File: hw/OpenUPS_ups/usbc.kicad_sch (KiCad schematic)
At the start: 12 parts, among them J1001 USB4105-GF-A, Q601 2N7002, U1001 MCP6547, U1002 AP22814BW5

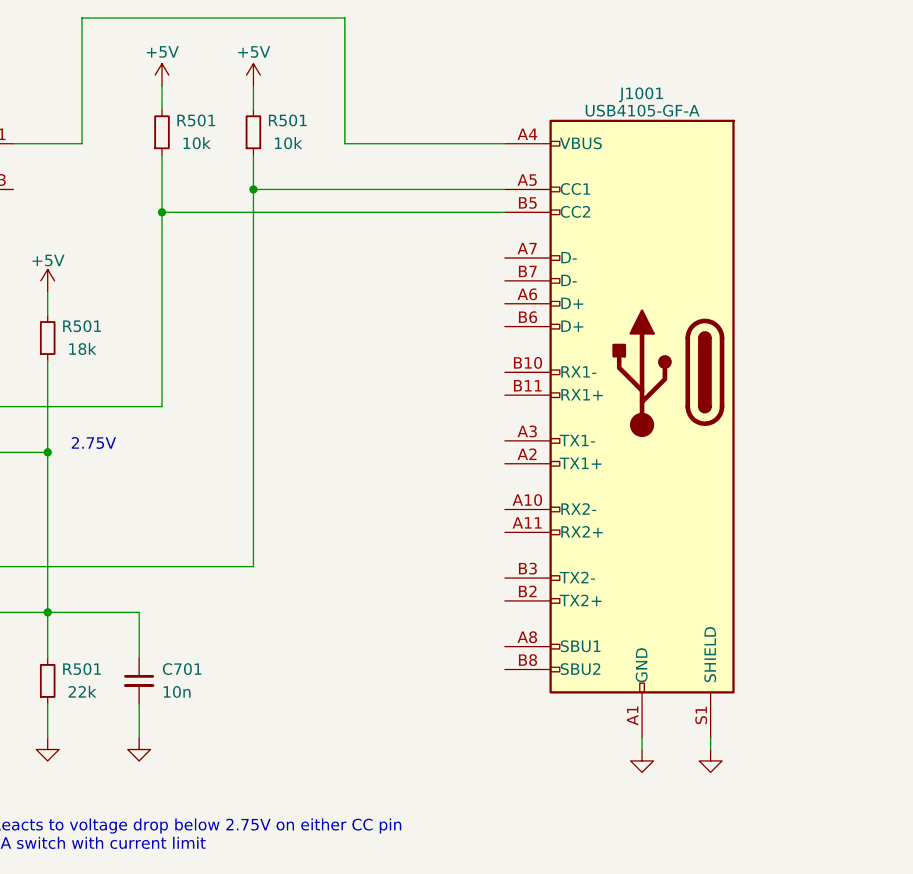
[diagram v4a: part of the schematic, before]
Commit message: Issue #22 ESD protection on USB, Bat Data, Fans
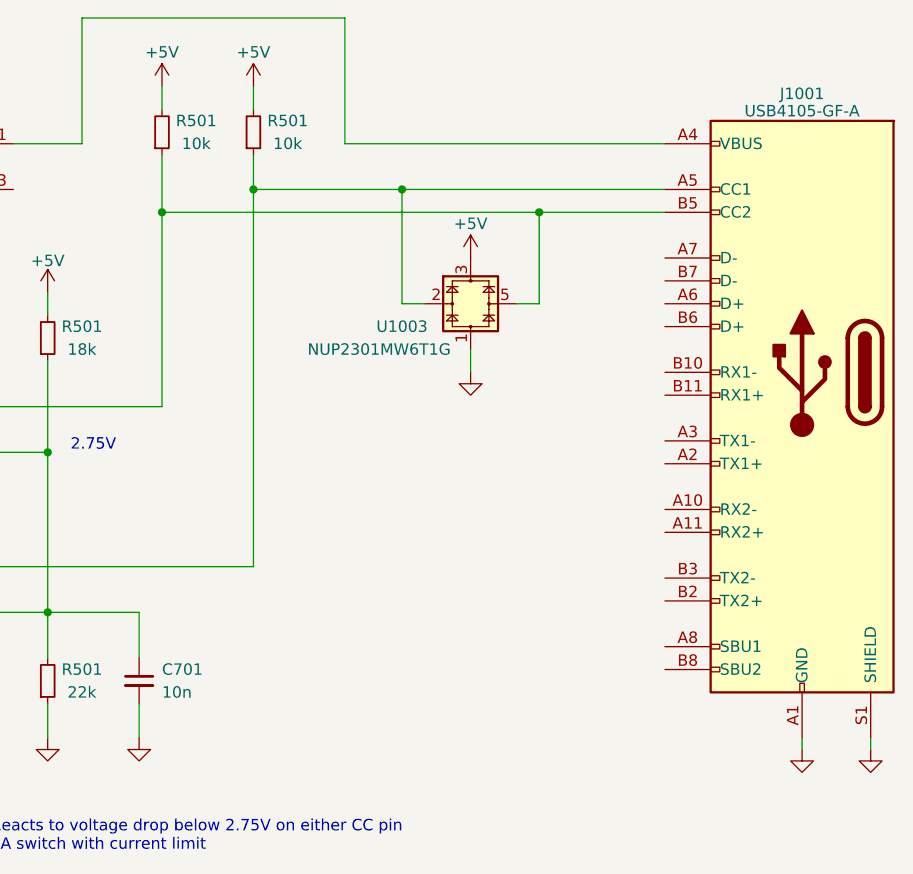
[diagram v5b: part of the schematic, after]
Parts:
- added U1003: NUP2301MW6T1G, Package_TO_SOT_SMD:SOT-363_SC-70-6, symbol OpenUPS_ups:NUP2301MW6T1G
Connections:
- net +5V: now also U1003.3
- net GND: now also U1003.1
- net at J1001.A5 (CC1), R501.1, U1001.5 (+): now also U1003.2
- net at J1001.B5 (CC2), R501.1, U1001.3 (+): now also U1003.5
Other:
- moved on the sheet: J1001
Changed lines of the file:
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@@
   (junction (at 66.04 80.01) (diameter 0) (color 0 0 0 0)
   )
+  (junction (at 137.16 35.56) (diameter 0) (color 0 0 0 0)
+  )
   (junction (at 66.04 38.1) (diameter 0) (color 0 0 0 0)
   )
@@
   (junction (at 97.79 64.77) (diameter 0) (color 0 0 0 0)
   )
+  (junction (at 152.4 38.1) (diameter 0) (color 0 0 0 0)
+  )
   (junction (at 66.04 27.94) (diameter 0) (color 0 0 0 0)
   )
@@
     (stroke (width 0) (type default))
   )
+  (wire (pts (xy 149.86 48.26) (xy 152.4 48.26))
+    (stroke (width 0) (type default))
+  )
   (wire (pts (xy 101.6 16.51) (xy 101.6 30.48))
     (stroke (width 0) (type default))
@@
     (stroke (width 0) (type default))
   )
+  (wire (pts (xy 137.16 35.56) (xy 166.37 35.56))
+    (stroke (width 0) (type default))
+  )
+  (wire (pts (xy 152.4 48.26) (xy 152.4 38.1))
+    (stroke (width 0) (type default))
+  )
   (wire (pts (xy 110.49 31.75) (xy 110.49 38.1))
     (stroke (width 0) (type default))
@@
     (stroke (width 0) (type default))
   )
-  (wire (pts (xy 148.59 30.48) (xy 130.81 30.48))
+  (wire (pts (xy 137.16 48.26) (xy 137.16 35.56))
+    (stroke (width 0) (type default))
+  )
+  (wire (pts (xy 166.37 30.48) (xy 130.81 30.48))
     (stroke (width 0) (type default))
   )
@@
     (stroke (width 0) (type default))
   )
-  (wire (pts (xy 163.83 96.52) (xy 163.83 97.79))
+  (wire (pts (xy 181.61 96.52) (xy 181.61 97.79))
     (stroke (width 0) (type default))
   )
@@
     (stroke (width 0) (type default))
   )
-  (wire (pts (xy 171.45 96.52) (xy 171.45 97.79))
+  (wire (pts (xy 189.23 96.52) (xy 189.23 97.79))
     (stroke (width 0) (type default))
   )
@@
     (stroke (width 0) (type default))
   )
+  (wire (pts (xy 139.7 48.26) (xy 137.16 48.26))
+    (stroke (width 0) (type default))
+  )
   (wire (pts (xy 107.95 87.63) (xy 107.95 82.55))
     (stroke (width 0) (type default))
@@
     (stroke (width 0) (type default))
   )
+  (wire (pts (xy 144.78 53.34) (xy 144.78 55.88))
+    (stroke (width 0) (type default))
+  )
   (wire (pts (xy 66.04 22.86) (xy 66.04 27.94))
     (stroke (width 0) (type default))
@@
     (stroke (width 0) (type default))
   )
-  (wire (pts (xy 120.65 35.56) (xy 148.59 35.56))
+  (wire (pts (xy 120.65 35.56) (xy 137.16 35.56))
     (stroke (width 0) (type default))
   )
@@
     (stroke (width 0) (type default))
   )
-  (wire (pts (xy 110.49 38.1) (xy 148.59 38.1))
+  (wire (pts (xy 110.49 38.1) (xy 152.4 38.1))
+    (stroke (width 0) (type default))
+  )
+  (wire (pts (xy 152.4 38.1) (xy 166.37 38.1))
     (stroke (width 0) (type default))
   )
@@
     )
   )
-  (symbol (lib_id "power:GND") (at 171.45 97.79 0) (unit 1)
-    (in_bom yes) (on_board yes) (dnp no)
-    (property "Reference" "#PWR0306" (at 171.45 104.14 0)
-      (effects (font (size 1.27 1.27)) hide)
-    )
-    (property "Value" "GND" (at 171.45 101.6 0)
-      (effects (font (size 1.27 1.27)) hide)
-    )
-    (property "Footprint" "" (at 171.45 97.79 0)
-      (effects (font (size 1.27 1.27)))
-    )
-    (property "Datasheet" "" (at 171.45 97.79 0)
+  (symbol (lib_id "power:GND") (at 189.23 97.79 0) (unit 1)
+    (in_bom yes) (on_board yes) (dnp no)
+    (property "Reference" "#PWR0306" (at 189.23 104.14 0)
+      (effects (font (size 1.27 1.27)) hide)
+    )
+    (property "Value" "GND" (at 189.23 101.6 0)
+      (effects (font (size 1.27 1.27)) hide)
+    )
+    (property "Footprint" "" (at 189.23 97.79 0)
+      (effects (font (size 1.27 1.27)))
+    )
+    (property "Datasheet" "" (at 189.23 97.79 0)
       (effects (font (size 1.27 1.27)))
     )
@@
     )
   )
+  (symbol (lib_id "power:+5V") (at 144.78 43.18 0) (unit 1)
+    (in_bom yes) (on_board yes) (dnp no)
+    (property "Reference" "#PWR0128" (at 144.78 46.99 0)
+      (effects (font (size 1.27 1.27)) hide)
+    )
+    (property "Value" "+5V" (at 144.78 39.37 0)
+      (effects (font (size 1.27 1.27)))
+    )
+    (property "Footprint" "" (at 144.78 43.18 0)
+      (effects (font (size 1.27 1.27)) hide)
+    )
+    (property "Datasheet" "" (at 144.78 43.18 0)
+      (effects (font (size 1.27 1.27)) hide)
+    )
+    (pin "1")
+    (instances
+      (project "OpenUPS_ups"
+        (path "/f77faec3-eac4-47f3-a2de-ec4a039f4502"
+          (reference "#PWR0128") (unit 1)
+        )
+        (path "/f77faec3-eac4-47f3-a2de-ec4a039f4502/5d533980-99bb-4871-b1d2-8a68cd48eb84"
+          (reference "#PWR01015") (unit 1)
+        )
+      )
+    )
+  )
+  (symbol (lib_id "power:GND") (at 144.78 55.88 0) (unit 1)
+    (in_bom yes) (on_board yes) (dnp no)
+    (property "Reference" "#PWR0306" (at 144.78 62.23 0)
+      (effects (font (size 1.27 1.27)) hide)
+    )
+    (property "Value" "GND" (at 144.78 59.69 0)
+      (effects (font (size 1.27 1.27)) hide)
+    )
+    (property "Footprint" "" (at 144.78 55.88 0)
+      (effects (font (size 1.27 1.27)))
+    )
+    (property "Datasheet" "" (at 144.78 55.88 0)
+      (effects (font (size 1.27 1.27)))
+    )
+    (pin "1")
+    (instances
+      (project "OpenUPS_ups"
+        (path "/f77faec3-eac4-47f3-a2de-ec4a039f4502/c1f639ea-b62e-4979-b175-523e44c4a4ee"
+          (reference "#PWR0306") (unit 1)
+        )
+        (path "/f77faec3-eac4-47f3-a2de-ec4a039f4502/0bd99307-a15c-41e8-997b-077d576f806c"
+          (reference "#PWR0514") (unit 1)
+        )
+        (path "/f77faec3-eac4-47f3-a2de-ec4a039f4502/8c312927-9c4e-41ad-b941-6f477a792759"
+          (reference "#PWR0805") (unit 1)
+        )
+        (path "/f77faec3-eac4-47f3-a2de-ec4a039f4502"
+          (reference "#PWR0129") (unit 1)
+        )
+        (path "/f77faec3-eac4-47f3-a2de-ec4a039f4502/5d533980-99bb-4871-b1d2-8a68cd48eb84"
+          (reference "#PWR01016") (unit 1)
+        )
+      )
+    )
+  )
   (symbol (lib_id "Device:R_Small") (at 120.65 29.21 0) (mirror x) (unit 1)
     (in_bom yes) (on_board yes) (dnp no)
@@
     )
   )
-  (symbol (lib_id "Connector:USB_C_Receptacle") (at 163.83 55.88 0) (mirror y) (unit 1)
-    (in_bom yes) (on_board yes) (dnp no)
-    (property "Reference" "J1001" (at 163.83 24.9301 0)
-      (effects (font (size 1.27 1.27)))
-    )
-    (property "Value" "USB4105-GF-A" (at 163.83 26.8511 0)
-      (effects (font (size 1.27 1.27)))
-    )
-    (property "Footprint" "Connector_USB:USB_C_Receptacle_GCT_USB4105-xx-A_16P_TopMnt_Horizontal" (at 160.02 55.88 0)
-      (effects (font (size 1.27 1.27)) hide)
-    )
-    (property "Datasheet" "" (at 160.02 55.88 0)
+  (symbol (lib_id "Connector:USB_C_Receptacle") (at 181.61 55.88 0) (mirror y) (unit 1)
+    (in_bom yes) (on_board yes) (dnp no)
+    (property "Reference" "J1001" (at 181.61 24.9301 0)
+      (effects (font (size 1.27 1.27)))
+    )
+    (property "Value" "USB4105-GF-A" (at 181.61 26.8511 0)
+      (effects (font (size 1.27 1.27)))
+    )
+    (property "Footprint" "Connector_USB:USB_C_Receptacle_GCT_USB4105-xx-A_16P_TopMnt_Horizontal" (at 177.8 55.88 0)
+      (effects (font (size 1.27 1.27)) hide)
+    )
+    (property "Datasheet" "" (at 177.8 55.88 0)
       (effects (font (size 1.27 1.27)) hide)
     )
@@
     )
   )
+  (symbol (lib_id "OpenUPS_ups:NUP2301MW6T1G") (at 144.78 44.45 0) (unit 1)
+    (in_bom yes) (on_board yes) (dnp no)
+    (property "Reference" "U1003" (at 137.16 50.8 0)
+      (effects (font (size 1.27 1.27)))
+    )
+    (property "Value" "NUP2301MW6T1G" (at 134.62 53.34 0)
+      (effects (font (size 1.27 1.27)))
+    )
+    (property "Footprint" "Package_TO_SOT_SMD:SOT-363_SC-70-6" (at 144.78 44.45 0)
+      (effects (font (size 1.27 1.27)) hide)
+    )
+    (property "Datasheet" "https://www.tme.eu/Document/58b5ad97e31b8cb20a2de836acc71031/NUP2301MW6T1G.PDF" (at 144.78 44.45 0)
+      (effects (font (size 1.27 1.27)) hide)
+    )
+    (pin "1")
+    (pin "2")
+    (pin "3")
+    (pin "4")
+    (pin "5")
+    (pin "6")
+    (instances
+      (project "OpenUPS_ups"
+        (path "/f77faec3-eac4-47f3-a2de-ec4a039f4502/5d533980-99bb-4871-b1d2-8a68cd48eb84"
+          (reference "U1003") (unit 1)
+        )
+      )
+    )
+  )
   (symbol (lib_id "power:GND") (at 83.82 44.45 0) (unit 1)
     (in_bom yes) (on_board yes) (dnp no)
@@
     )
   )
-  (symbol (lib_id "power:GND") (at 163.83 97.79 0) (unit 1)
-    (in_bom yes) (on_board yes) (dnp no)
-    (property "Reference" "#PWR0306" (at 163.83 104.14 0)
-      (effects (font (size 1.27 1.27)) hide)
-    )
-    (property "Value" "GND" (at 163.83 101.6 0)
-      (effects (font (size 1.27 1.27)) hide)
-    )
-    (property "Footprint" "" (at 163.83 97.79 0)
-      (effects (font (size 1.27 1.27)))
-    )
-    (property "Datasheet" "" (at 163.83 97.79 0)
-      (effects (font (size 1.27 1.27)))
-    )
+  (symbol (lib_id "power:GND") (at 181.61 97.79 0) (unit 1)
+    (in_bom yes) (on_board yes) (dnp no)
+    (property "Reference" "#PWR0306" (at 181.61 104.14 0)
+      (effects (font (size 1.27 1.27)) hide)
+    )
+    (property "Value" "GND" (at 181.61 101.6 0)
+      (effects (font (size 1.27 1.27)) hide)
+    )
+    (property "Footprint" "" (at 181.61 97.79 0)
+      (effects (font (size 1.27 1.27)))
+    )
+    (property "Datasheet" "" (at 181.61 97.79 0)
+      (effects (font (size 1.27 1.27)))
+    )
